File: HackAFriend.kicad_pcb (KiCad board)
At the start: 2 copper layers, 135 x 59 mm, 101 parts, among them J1 PRT-14417, J10 Conn_01x16, J3 Conn_01x02, J4 Conn_01x02, J5 Conn_01x02, J6 10152803-00011LF, J7 Conn_01x02, J8 Conn_01x12, J9 Conn_01x02, P1 TC2050-IDC, SW1 GP0115ACCG30, SW10 SPST_BTN_A, SW11 SPST_BTN_X, SW12 SPST_BTN_Y, SW2 SW_SPST, SW3 SPST_DPAD_LEFT, SW4 SPST_BTN_SELECT, SW5 SPST_DPAD_DOWN, SW6 SPST_DPAD_RIGHT, SW7 SPST_DPAD_UP, SW8 SPST_DPAD_START, SW9 SPST_BTN_B, U1 DA7282-00FVC, U3 W25Q64JVSSIQ, U4 MCP23017_ML, U6 BQ24072RGT, U7 MAX98357A, U8 NJM2884U1-33-TE1, U9 MDBT50Q-1MV2, Y1 ABS06-32.768KHZ-1-T

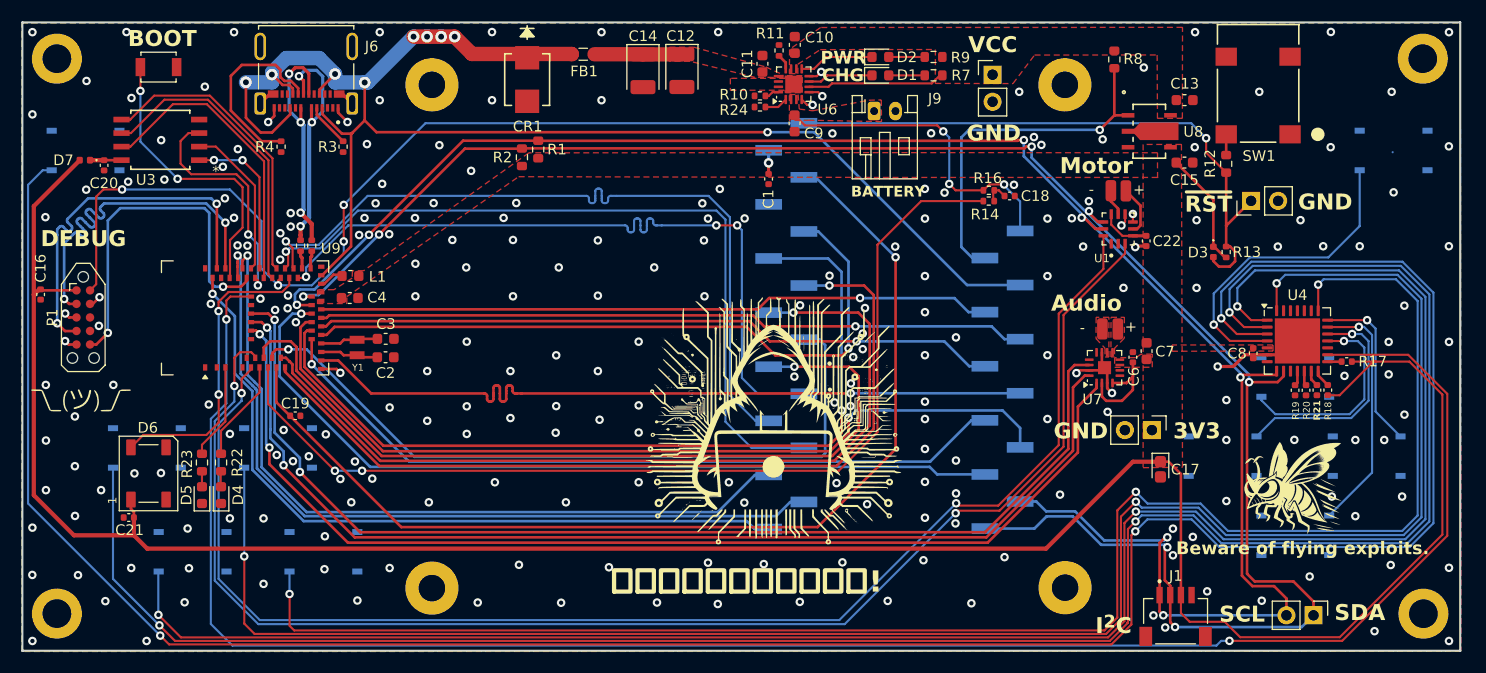
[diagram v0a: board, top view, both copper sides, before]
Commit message: Release candidate
Changed USBC connector, changed TagConnect to use footprint with legs, move NRF52 to edge of board, clean up traces
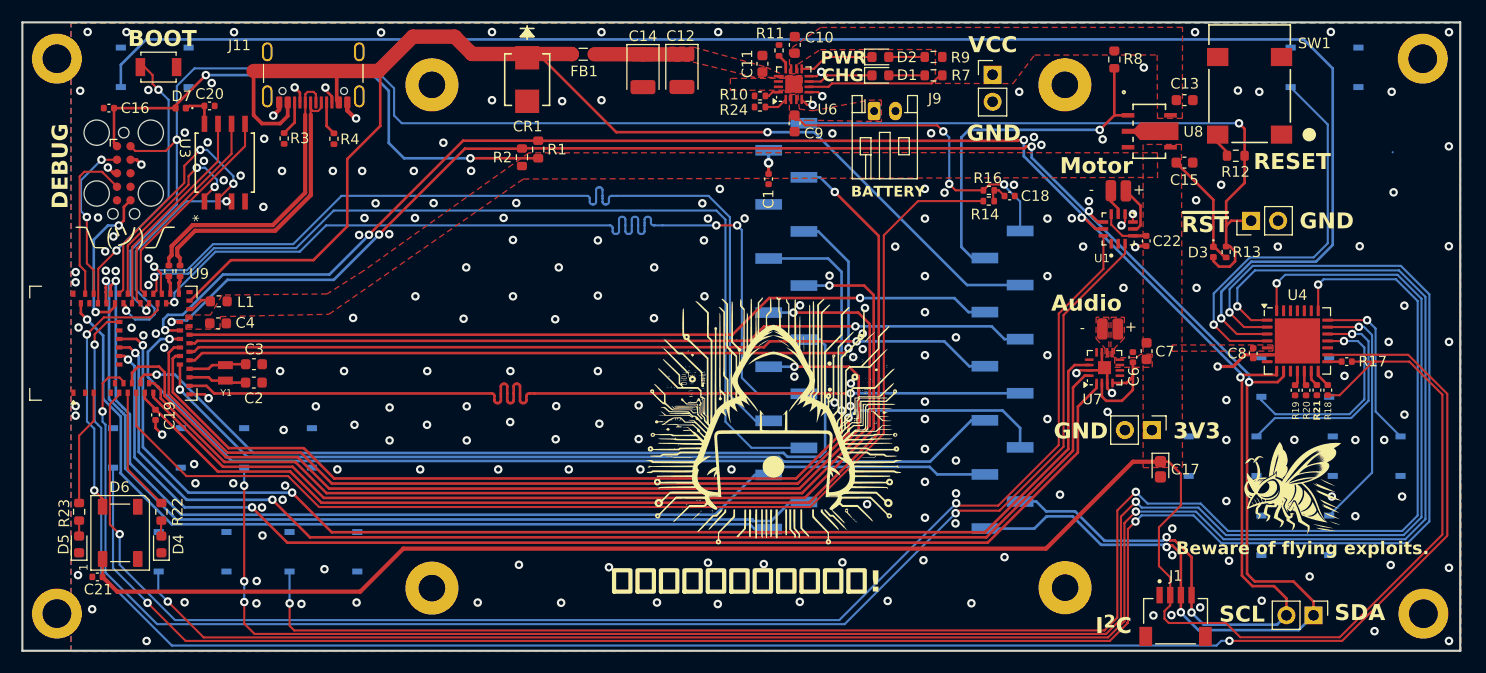
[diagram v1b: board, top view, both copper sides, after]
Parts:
- removed J6: 10152803-00011LF, 10152803_00011LF:AMPHENOL_10152803-00011LF
- added J11: USB_C_Receptacle_USB2.0_16P, Connector_USB:USB_C_Receptacle_GCT_USB4105-xx-A_16P_TopMnt_Horizontal, F.Cu at (108.4, 65.3)
- P1: footprint Connector:Tag-Connect_TC2050-IDC-NL_2x05_P1.27mm_Vertical -> Connector:Tag-Connect_TC2050-IDC-FP_2x05_P1.27mm_Vertical
- moved C16 18.6 mm to (89.2, 69.5), turned to 180 degrees
- moved G*** 15.8 mm to (90.8, 81.5)
- moved P1 14.1 mm to (90.6, 75.6)
- moved C19 13.1 mm to (93.6, 98.3), turned to -90 degrees
- moved L1 12.6 mm to (99.5, 87.7)
- moved U9 12.6 mm to (89.6, 91.6)
- moved Y1 12.6 mm to (100.1, 94.4)
- moved C2 12.6 mm to (102.8, 95.3)
- moved C3 12.6 mm to (102.8, 93.6)
- moved C4 12.6 mm to (99.4, 89.7)
- moved R5 12.6 mm to (94.8, 84.8)
- moved R6 12.6 mm to (95.9, 84.8)
- moved D5 12.4 mm to (86.4, 110.5)
- moved R23 12.4 mm to (86.4, 107.4)
- moved C20 11.4 mm to (98.6, 69.3), turned to 0 degrees
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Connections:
- J1 pad 1: /Connectors/I2C_BUS.SCL -> GND
- J1 pad 2: /Connectors/I2C_BUS.SDA -> +3V3
- J1 pad 3: +3V3 -> /Connectors/I2C_BUS.SDA
- J1 pad 4: GND -> /Connectors/I2C_BUS.SCL
- R3 pad 1: GND -> Net-(J11-CC2)
- R3 pad 2: Net-(J6-CC1) -> GND
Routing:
- net /Human Interfaces/BTN_SELECT: track 233.3 -> 154.3 mm, vias 3 -> 1
- net /Connectors/CORESIGHT.SWDIO: track 34.8 -> 15.3 mm
- net /Connectors/CORESIGHT.SWDCLK: track 34.9 -> 15.5 mm, vias 2 -> 0
- net /Connectors/CORESIGHT.SWO: track 33.5 -> 14.9 mm
- net /MCU/SCK: track 68.8 -> 86.1 mm
- net /MCU/VBAT_MEAS: track 94.0 -> 108.6 mm, vias 2 -> 0
- net Net-(J11-CC1): track 17.8 -> 3.18 mm
- net /MCU/D10: track 71.9 -> 85.9 mm
- net /MCU/A1: track 80.4 -> 94.3 mm
- net /MCU/A5: track 77.7 -> 91.6 mm
- net /MCU/D6: track 80.8 -> 94.7 mm
- net /MCU/A3: track 80.6 -> 94.5 mm
- net /MCU/A2: track 80.3 -> 94.1 mm
- net /Connectors/USB_VBUS: track 146.7 -> 132.9 mm, vias 9 -> 1
- net /MCU/MOSI: track 71.9 -> 85.5 mm
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
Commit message: Change button footprint
Change button footprint to PTS647 and add a few more stitching vias.
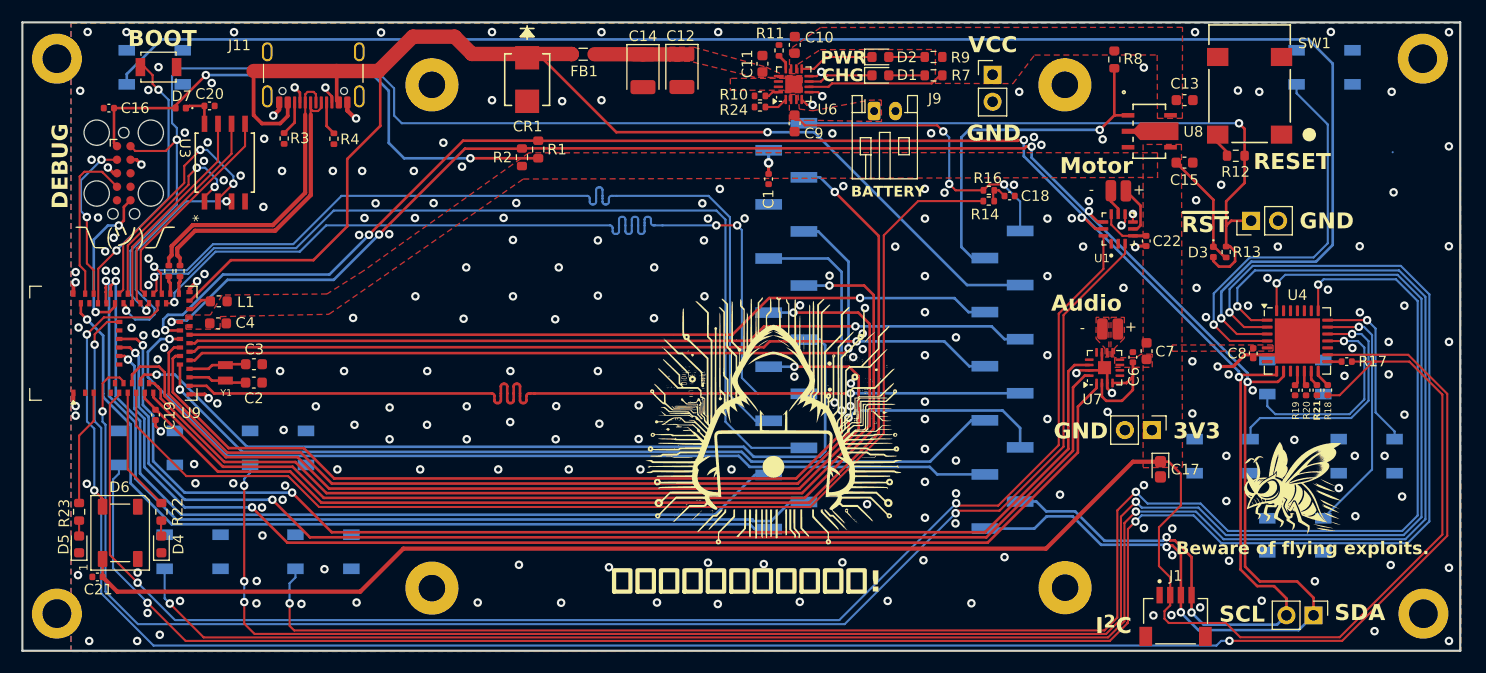
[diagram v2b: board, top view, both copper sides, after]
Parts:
- SW10, SW11, SW12, SW3, SW4, SW5, SW6, SW7, SW8, SW9: footprint PTS526_SK15_SMTR2_LFS:SMT_FS -> PTS_647_SN50_SMTR2_LFS:SW_PTS_647_SN50_SMTR2_LFS
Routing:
- net GND: track 35.0 -> 38.5 mm, vias 226 -> 248
- net /Human Interfaces/DPAD_LEFT: track 21.6 -> 22.9 mm
- net /Connectors/~{RESET}: track 153.2 -> 154.3 mm
- net /Human Interfaces/BTN_SELECT: track 154.3 -> 153.2 mm
- net /Human Interfaces/MOTOR_DRV.GPI0: track 140.7 -> 141.7 mm
- net /Human Interfaces/~{INPUT_IRQ}: track 185.1 -> 186.1 mm

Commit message: Update part numbers
Update part numbers for 12 and 16 PIN SMD 2.54mm pins and USB-C 2.0 connector.
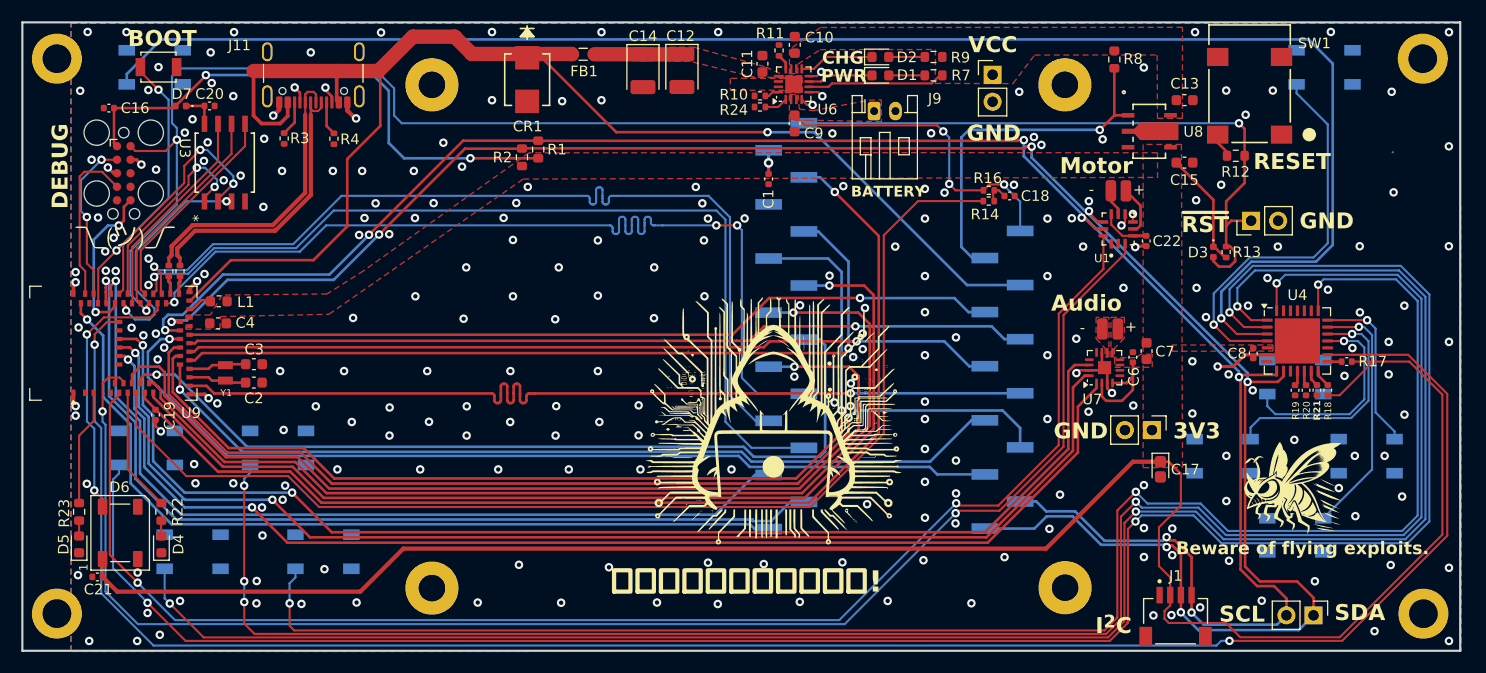
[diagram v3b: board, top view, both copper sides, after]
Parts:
- moved D7 0.20 mm to (95.9, 69.3)
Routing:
- net GND: vias 248 -> 259
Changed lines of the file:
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@@
 	(footprint "Diode_SMD:D_0402_1005Metric"
 		(layer "F.Cu")
-		(at 95.9248 69.53 180)
+		(at 95.9248 69.33 180)
 		(descr "Diode SMD 0402 (1005 Metric), square (rectangular) end terminal, IPC_7351 nominal, (Body size source: http://www.tortai-tech.com/upload/download/2011102023233369053.pdf), generated with kicad-footprint-generator")
 		(tags "diode")
@@
 			)
 		)
+		(property "MP" "USB4105-GF-A"
+			(at 0 0 180)
+			(unlocked yes)
+			(layer "F.Fab")
+			(hide yes)
+			(effects
+				(font
+					(size 1 1)
+					(thickness 0.15)
+				)
+			)
+		)
 		(property ki_fp_filters "USB*C*Receptacle*")
 		(sheetname "/Connectors/")
@@
 			)
 		)
-		(property "Datasheet" "https://www.we-online.com/components/products/datasheet/61301211121.pdf"
+		(property "Datasheet" "https://www.te.com/usa-en/product-1-1241150-2.datasheet.pdf"
 			(at 0 0 0)
 			(unlocked yes)
@@
 			)
 		)
-		(property "MP" "M20-8771246"
+		(property "MP" "1-1241150-2"
 			(at 0 0 180)
 			(unlocked yes)
@@
 			)
 		)
-		(property "Datasheet" "https://www.we-online.com/components/products/datasheet/61301611121.pdf"
+		(property "Datasheet" "https://suddendocs.samtec.com/catalog_english/tsm.pdf"
 			(at 0 0 0)
 			(unlocked yes)
@@
 			)
 		)
-		(property "MP" "M20-8771642R"
+		(property "MP" "TSM-116-01-T-SV-P-TR"
 			(at 0 0 180)
 			(unlocked yes)
@@
 	)
 	(gr_text "PWR"
-		(at 155.9898 65.5 0)
+		(at 156.0348 67.205 0)
 		(layer "F.SilkS")
 		(effects
@@
 	)
 	(gr_text "CHG"
-		(at 156.1298 67.15 0)
+		(at 156.1298 65.505 0)
 		(layer "F.SilkS")
 		(effects
@@
 	)
 	(segment
-		(start 98.2848 66.43)
-		(end 95.4398 69.275)
+		(start 98.2848 66.48)
+		(end 95.4398 69.325)
 		(width 0.25)
 		(layer "F.Cu")
@@
 	)
 	(segment
-		(start 95.4398 69.53)
-		(end 89.6598 69.53)
-		(width 0.25)
-		(layer "F.Cu")
-		(net 1)
-	)
-	(segment
 		(start 177.1698 110.89)
 		(end 185.3298 102.73)
@@
 	)
 	(segment
-		(start 95.4398 69.275)
-		(end 95.4398 69.55)
-		(width 0.25)
-		(layer "F.Cu")
-		(net 1)
-	)
-	(segment
 		(start 89.6598 69.53)
 		(end 89.6598 72.824)
@@
 	)
 	(segment
+		(start 98.2848 66.43)
+		(end 98.2848 66.48)
+		(width 0.25)
+		(layer "F.Cu")
+		(net 1)
+	)
+	(segment
 		(start 211.2798 93.33)
 		(end 214.3798 96.43)
@@
 	)
 	(segment
+		(start 95.2398 69.53)
+		(end 89.6598 69.53)
+		(width 0.25)
+		(layer "F.Cu")
+		(net 1)
+	)
+	(segment
+		(start 95.4398 69.33)
+		(end 95.2398 69.53)
+		(width 0.25)
+		(layer "F.Cu")
+		(net 1)
+	)
+	(segment
 		(start 188.6798 102.73)
 		(end 189.8298 103.88)
@@
 	)
 	(segment
+		(start 95.4398 69.325)
+		(end 95.4398 69.33)
+		(width 0.25)
+		(layer "F.Cu")
+		(net 1)
+	)
+	(segment
 		(start 204.7298 96.49)
 		(end 207.8898 93.33)
@@
 	)
 	(via
-		(at 131.1298 100.62)
+		(at 131.1196 100.275)
 		(size 0.8)
 		(drill 0.4)
@@
 	)
 	(via
+		(at 185.3598 97.455)
+		(size 0.8)
+		(drill 0.4)
+		(layers "F.Cu" "B.Cu")
+		(net 2)
+	)
+	(via
 		(at 179.589104 79.874205)
 		(size 0.8)
@@
 	)
 	(via
+		(at 180.0098 91.18)
+		(size 0.8)
+		(drill 0.4)
+		(layers "F.Cu" "B.Cu")
+		(net 2)
+	)
+	(via
 		(at 90.8298 62.39)
 		(size 0.8)
@@
 	)
 	(via
-		(at 182.9498 98.05)
+		(at 181.1598 98.03)
 		(size 0.8)
 		(drill 0.4)
@@
 	)
 	(via
+		(at 98.7348 64.3)
+		(size 0.8)
+		(drill 0.4)
+		(layers "F.Cu" "B.Cu")
+		(net 2)
+	)
+	(via
 		(at 94.0598 99.88)
 		(size 0.8)
@@
 	)
 	(via
-		(at 146.5398 77.12)
+		(at 177.4848 109.03)
+		(size 0.8)
+		(drill 0.4)
+		(layers "F.Cu" "B.Cu")
+		(net 2)
+	)
+	(via
+		(at 144.2848 76.93)
+		(size 0.8)
+		(drill 0.4)
+		(layers "F.Cu" "B.Cu")
+		(net 2)
+	)
+	(via
+		(at 108.1348 64.3)
 		(size 0.8)
 		(drill 0.4)
@@
 	)
 	(via
-		(at 135.2298 99.165)
+		(at 135.2298 99)
 		(size 0.8)
 		(drill 0.4)
@@
 	)
 	(via
-		(at 119.0498 99.265)
+		(at 119.2348 98.98)
 		(size 0.8)
 		(drill 0.4)
@@
 	)
 	(via
-		(at 197.1898 68)
+		(at 198.4598 67.88)
 		(size 0.8)
 		(drill 0.4)
@@
 	)
 	(via
-		(at 122.7798 100.62)
+		(at 122.7696 100.275)
 		(size 0.8)
 		(drill 0.4)
@@
 	)
 	(via
-		(at 195.1848 67.88)
+		(at 194.0848 67.88)
+		(size 0.8)
+		(drill 0.4)
+		(layers "F.Cu" "B.Cu")
+		(net 2)
+	)
+	(via
+		(at 93.6098 75.305)
 		(size 0.8)
 		(drill 0.4)
@@
 	)
 	(via
-		(at 115.5348 100.62)
+		(at 115.5246 100.275)
 		(size 0.8)
 		(drill 0.4)
@@
 	)
 	(via
-		(at 126.8598 99.005)
+		(at 126.8598 99)
 		(size 0.8)
 		(drill 0.4)
@@
 	)
 	(via
-		(at 112.2398 99.265)
+		(at 111.9848 99)
 		(size 0.8)
 		(drill 0.4)
@@
 	)
 	(via
+		(at 100.8598 68.405)
+		(size 0.8)
+		(drill 0.4)
+		(layers "F.Cu" "B.Cu")
+		(net 2)
+	)
+	(via
 		(at 96.3098 71.83)
 		(size 0.8)
@@
 	)
 	(via
-		(at 138.92 100.6)
+		(at 138.9098 100.255)
 		(size 0.8)
 		(drill 0.4)
@@
 	)
 	(via
+		(at 128.5098 76.93)
+		(size 0.8)
+		(drill 0.4)
+		(layers "F.Cu" "B.Cu")
+		(net 2)
+	)
+	(via
 		(at 186.3598 108.955)
 		(size 0.8)
@@
 	)
 	(via
+		(at 97.0348 70.58)
+		(size 0.8)
+		(drill 0.4)
+		(layers "F.Cu" "B.Cu")
+		(net 2)
+	)
+	(via
 		(at 87.557797 74.38)
 		(size 0.8)
@@
 	)
 	(via
+		(at 186.3598 111.68)
+		(size 0.8)
+		(drill 0.4)
+		(layers "F.Cu" "B.Cu")
+		(net 2)
+	)
+	(via
 		(at 103.6848 78.805)
 		(size 0.8)
@@
 	)
 	(via
+		(at 195.9098 70.155)
+		(size 0.8)
+		(drill 0.4)
+		(layers "F.Cu" "B.Cu")
+		(net 2)
+	)
+	(via
 		(at 194.1 106.42)
 		(size 0.8)
@@
 	)
 	(segment
-		(start 92.5348 65.68)
-		(end 92.1398 65.68)
-		(width 0.2)
-		(layer "F.Cu")
-		(net 54)
-	)
-	(segment
 		(start 88.183032 84.606768)
 		(end 88.183032 87.823047)
@@
 	)
 	(segment
-		(start 93.2848 66.43)
-		(end 92.5348 65.68)
-		(width 0.2)
-		(layer "F.Cu")
-		(net 54)
-	)
-	(segment
-		(start 93.2848 67.255)
-		(end 93.2848 66.43)
+		(start 92.1398 66.11)
+		(end 92.1398 65.68)
 		(width 0.2)
 		(layer "F.Cu")
@@
 	(segment
 		(start 93.8348 67.805)
-		(end 93.2848 67.255)
+		(end 92.1398 66.11)
 		(width 0.2)
 		(layer "F.Cu")
@@
 	)
 	(segment
-		(start 102.7668 70.197)
-		(end 102.7668 66.047)
+		(start 105.2598 70.98)
+		(end 103.5098 70.98)
 		(width 0.35)
 		(layer "F.Cu")
@@
 	)
 	(segment
-		(start 105.9698 69)
-		(end 105.9698 70.27)
-		(width 0.35)
-		(layer "F.Cu")
-		(net 65)
-	)
-	(segment
-		(start 103.5498 70.98)
-		(end 102.7668 70.197)
+		(start 102.7598 70.23)
+		(end 102.7598 66.054)
 		(width 0.35)
 		(layer "F.Cu")
@@
 	)
 	(segment
-		(start 105.9698 70.27)
-		(end 105.2598 70.98)
+		(start 105.9698 69)
+		(end 105.9698 70.27)
 		(width 0.35)
 		(layer "F.Cu")
@@
 	)
 	(segment
-		(start 105.2598 70.98)
-		(end 103.5498 70.98)
-		(width 0.35)
-		(layer "F.Cu")
-		(net 65)
-	)
-	(segment
 		(start 114.6598 71.205)
 		(end 111.5598 74.305)
@@
 	)
 	(segment
+		(start 105.9698 70.27)
+		(end 105.2598 70.98)
+		(width 0.35)
+		(layer "F.Cu")
+		(net 65)
+	)
+	(segment
 		(start 117.717 62.8228)
 		(end 114.4928 66.047)
@@
 	)
 	(segment
+		(start 103.5098 70.98)
+		(end 102.7598 70.23)
+		(width 0.35)
+		(layer "F.Cu")
+		(net 65)
+	)
+	(segment
 		(start 110.5348 66.047)
 		(end 102.7668 66.047)
@@
 	)
 	(segment
-		(start 96.7399 69.3249)
-		(end 96.4098 69.655)
+		(start 98.1498 69.3249)
+		(end 96.7399 69.3249)
+		(width 0.25)
+		(layer "F.Cu")
+		(net 131)
+	)
+	(segment
+		(start 96.7348 69.33)
+		(end 96.4098 69.33)
 		(width 0.25)
 		(layer "F.Cu")
@@
 	)
 	(segment
-		(start 98.1498 69.3249)
-		(end 98.1498 71)
+		(start 96.7399 69.3249)
+		(end 96.7348 69.33)
 		(width 0.25)
 		(layer "F.Cu")
@@
 	(segment
 		(start 98.1498 69.3249)
-		(end 96.7399 69.3249)
+		(end 98.1498 71)
 		(width 0.25)
 		(layer "F.Cu")

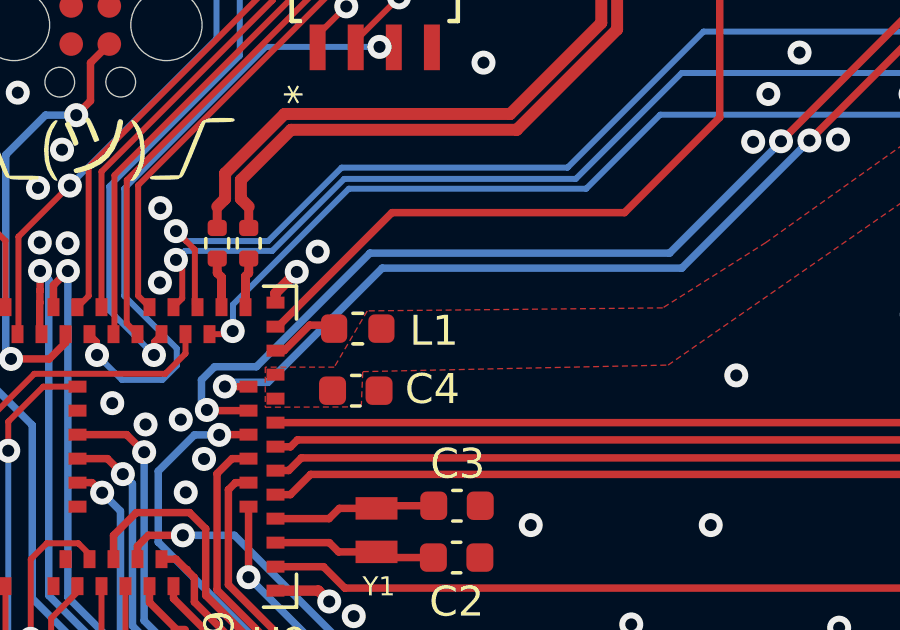
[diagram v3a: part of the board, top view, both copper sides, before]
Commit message: Add bypass capacitor
Added bypass capacitor on VBUS for MCU
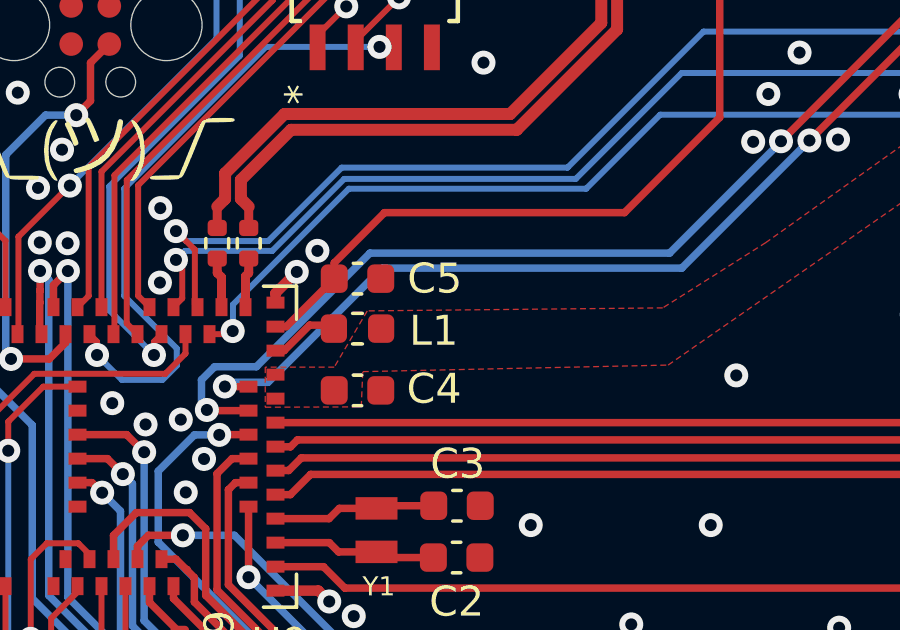
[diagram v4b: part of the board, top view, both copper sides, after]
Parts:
- added C5: 10uF, Capacitor_SMD:C_0603_1608Metric, F.Cu at (99.5, 86.0)
- moved C4 0.06 mm to (99.5, 89.7)
